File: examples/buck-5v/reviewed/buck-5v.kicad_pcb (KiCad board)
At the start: 2 copper layers, 126 x 56 mm, 11 parts, among them J1 12V IN, J2 5V OUT, U1 LM2596S-5

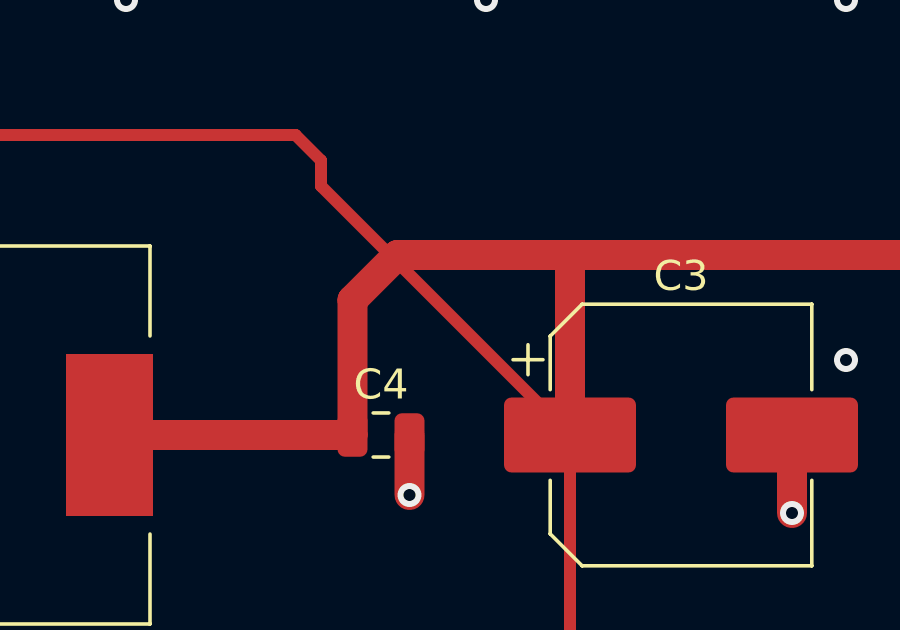
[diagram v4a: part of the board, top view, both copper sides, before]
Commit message: A net may not cross its own copper
The reviewer looked at the plots, saw tracks driven through each other, and
asked whether the other checks were really passing. Both halves of the
answer were worth keeping. Measured directly - every pair of same-layer
segments on every reviewed board - there is not one crossing between
different nets: DRC reports zero errors, zero shorts, zero unconnected, and
it is not being fooled. What the plots show is a net crossing *itself*:
thirteen places on the FPGA board, one each on the op-amp and the buck.
Same potential, so DRC has nothing to say; no length ratio catches it; no
rule of ours looked. The checks were honest. The check list had a hole
exactly the shape of what the eye catches first.

route.self_crossing (new, warning, promoted by ai-generated) measures it:
two branches of one net crossing means the copper carries a redundant loop,
and a person never draws one. KiCad's demo corpus: 6 of 16 boards carry one
to three, at dense escapes.

_unlooped (new pass) is the fix, as a graph question: split every same-net
crossing so the X is a node, and while any cycle remains in the net's
copper, remove the longest junction-to-junction chain of the cycle -
connectivity is kept by definition, a cycle has two ways round, and the
amputated X becomes an ordinary corner. The clearance oracle now also
refuses to let _doglegged or _straighten draw a new X over their own net.

The cutter was wrong twice before it was right, both times the same lesson:
KiCad's connectivity is geometric, a track graph is endpoint topology, and
the difference is exactly a pad. The escape fan draws a micro-hook inside
an off-grid pad - the overlap is the connection - and the graph read it as
a dangling loop and amputated the pad's only feed. Nodes inside an own-net
pad are anchors now, a cycle wholly inside one pad is immune, and segments
passing over a pad are split so the feed is a node the cut must respect.

Self-crossings on the five reviewed boards: 0/0/0/0/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
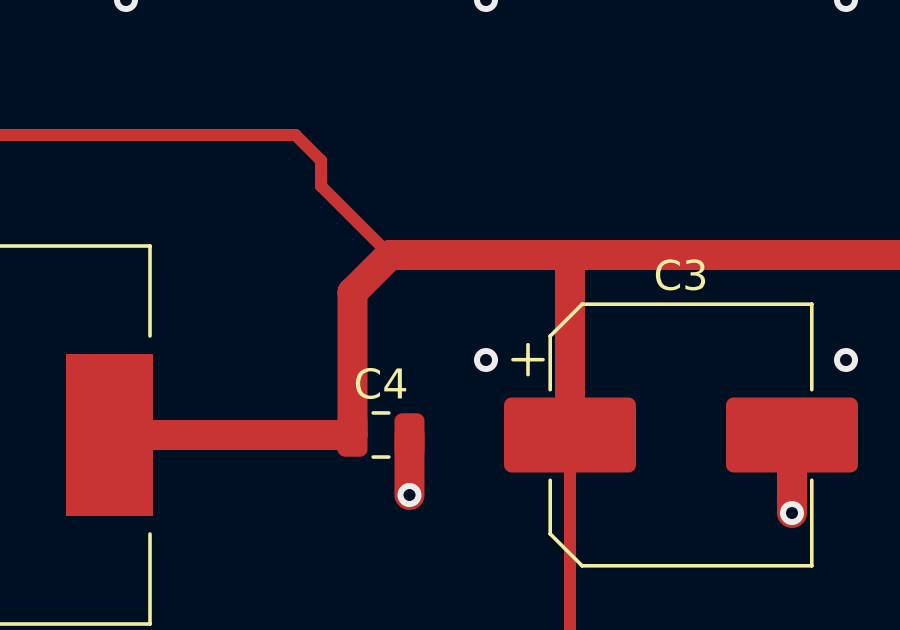
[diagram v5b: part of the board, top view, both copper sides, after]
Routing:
- net /+5V: track 131.6 -> 123.3 mm
- net GND: vias 84 -> 85
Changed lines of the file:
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@@
 	(gr_line (start 226.0 116.0) (end 100.0 116.0) (stroke (width 0.1) (type default)) (layer "Edge.Cuts"))
 	(gr_line (start 100.0 116.0) (end 100.0 60.0) (stroke (width 0.1) (type default)) (layer "Edge.Cuts"))
+	(segment (start 110.0 77.0) (end 110.0 108.5) (width 1.0) (layer "F.Cu") (net 1))
+	(segment (start 110.0 108.5) (end 111.5 110.0) (width 1.0) (layer "F.Cu") (net 1))
+	(segment (start 111.5 110.0) (end 116.0 110.0) (width 1.0) (layer "F.Cu") (net 1))
+	(segment (start 116.0 110.0) (end 210.0 110.0) (width 1.0) (layer "F.Cu") (net 1))
+	(segment (start 210.0 110.0) (end 219.5 110.0) (width 1.0) (layer "F.Cu") (net 1))
+	(segment (start 219.5 110.0) (end 221.0 108.5) (width 1.0) (layer "F.Cu") (net 1))
+	(segment (start 221.0 108.5) (end 221.0 96.0) (width 1.0) (layer "F.Cu") (net 1))
+	(segment (start 221.0 96.0) (end 216.0 91.0) (width 1.0) (layer "F.Cu") (net 1))
+	(segment (start 154.35 72.0) (end 151.0 72.0) (width 1.0) (layer "F.Cu") (net 1))
+	(segment (start 154.35 75.4) (end 154.35 80.0) (width 1.0) (layer "F.Cu") (net 1))
+	(segment (start 163.5 72.0) (end 163.5 80.0) (width 1.0) (layer "F.Cu") (net 1))
+	(segment (start 135.7 72.0) (end 135.7 74.6) (width 1.0) (layer "F.Cu") (net 1))
+	(segment (start 150.0 66.05) (end 150.0 64.4) (width 1.0) (layer "F.Cu") (net 1))
+	(segment (start 160.0 96.0) (end 160.0 91.0) (width 1.0) (layer "F.Cu") (net 1))
+	(segment (start 190.95 96.0) (end 190.95 98.0) (width 1.0) (layer "F.Cu") (net 1))
+	(segment (start 203.7 96.0) (end 203.7 98.6) (width 1.0) (layer "F.Cu") (net 1))
+	(segment (start 207.9375 106.0) (end 207.938 110.0) (width 0.4) (layer "F.Cu") (net 1))
 	(segment (start 110.0 72.0) (end 118.0 64.0) (width 1.0) (layer "F.Cu") (net 2))
 	(segment (start 118.0 64.0) (end 128.3 64.0) (width 1.0) (layer "F.Cu") (net 2))
@@
 	(segment (start 187.15 86.0) (end 188.0 86.85) (width 0.4) (layer "F.Cu") (net 3))
 	(segment (start 188.0 86.85) (end 188.0 87.7) (width 0.4) (layer "F.Cu") (net 3))
-	(segment (start 188.0 87.7) (end 196.3 96.0) (width 0.4) (layer "F.Cu") (net 3))
+	(segment (start 188.0 87.7) (end 190.3 90.0) (width 0.4) (layer "F.Cu") (net 3))
 	(segment (start 180.95 96.0) (end 189.05 96.0) (width 1.0) (layer "F.Cu") (net 3))
-	(segment (start 189.05 96.0) (end 189.05 91.5) (width 1.0) (layer "F.Cu") (net 3))
-	(segment (start 189.05 91.5) (end 190.55 90.0) (width 1.0) (layer "F.Cu") (net 3))
-	(segment (start 190.55 90.0) (end 196.3 90.0) (width 1.0) (layer "F.Cu") (net 3))
+	(segment (start 189.05 96.0) (end 189.05 91.25) (width 1.0) (layer "F.Cu") (net 3))
+	(segment (start 189.05 91.25) (end 190.3 90.0) (width 1.0) (layer "F.Cu") (net 3))
+	(segment (start 190.3 90.0) (end 196.3 90.0) (width 1.0) (layer "F.Cu") (net 3))
 	(segment (start 196.3 90.0) (end 196.3 96.0) (width 1.0) (layer "F.Cu") (net 3))
 	(segment (start 196.3 90.0) (end 210.0 90.0) (width 1.0) (layer "F.Cu") (net 3))
@@
 	(segment (start 196.3 103.2125) (end 199.0875 106.0) (width 0.4) (layer "F.Cu") (net 3))
 	(segment (start 200.9125 106.0) (end 206.0625 106.0) (width 0.4) (layer "F.Cu") (net 4))
-	(segment (start 110.0 77.0) (end 110.0 108.5) (width 1.0) (layer "F.Cu") (net 1))
-	(segment (start 110.0 108.5) (end 111.5 110.0) (width 1.0) (layer "F.Cu") (net 1))
-	(segment (start 111.5 110.0) (end 116.0 110.0) (width 1.0) (layer "F.Cu") (net 1))
-	(segment (start 116.0 110.0) (end 210.0 110.0) (width 1.0) (layer "F.Cu") (net 1))
-	(segment (start 210.0 110.0) (end 219.5 110.0) (width 1.0) (layer "F.Cu") (net 1))
-	(segment (start 219.5 110.0) (end 221.0 108.5) (width 1.0) (layer "F.Cu") (net 1))
-	(segment (start 221.0 108.5) (end 221.0 96.0) (width 1.0) (layer "F.Cu") (net 1))
-	(segment (start 221.0 96.0) (end 216.0 91.0) (width 1.0) (layer "F.Cu") (net 1))
-	(segment (start 154.35 72.0) (end 151.0 72.0) (width 1.0) (layer "F.Cu") (net 1))
-	(segment (start 154.35 75.4) (end 154.35 80.0) (width 1.0) (layer "F.Cu") (net 1))
-	(segment (start 163.5 72.0) (end 163.5 80.0) (width 1.0) (layer "F.Cu") (net 1))
-	(segment (start 135.7 72.0) (end 135.7 74.6) (width 1.0) (layer "F.Cu") (net 1))
-	(segment (start 150.0 66.05) (end 150.0 64.4) (width 1.0) (layer "F.Cu") (net 1))
-	(segment (start 160.0 96.0) (end 160.0 91.0) (width 1.0) (layer "F.Cu") (net 1))
-	(segment (start 190.95 96.0) (end 190.95 98.0) (width 1.0) (layer "F.Cu") (net 1))
-	(segment (start 203.7 96.0) (end 203.7 98.6) (width 1.0) (layer "F.Cu") (net 1))
-	(segment (start 207.9375 106.0) (end 207.938 110.0) (width 0.4) (layer "F.Cu") (net 1))
 	(via (at 169.5 67.5) (size 0.8) (drill 0.4) (layers "F.Cu" "B.Cu") (net 1))
 	(via (at 169.5 72.0) (size 0.8) (drill 0.4) (layers "F.Cu" "B.Cu") (net 1))
@@
 	(via (at 145.5 93.5) (size 0.8) (drill 0.4) (layers "F.Cu" "B.Cu") (net 1))
 	(via (at 157.5 93.5) (size 0.8) (drill 0.4) (layers "F.Cu" "B.Cu") (net 1))
+	(via (at 193.5 93.5) (size 0.8) (drill 0.4) (layers "F.Cu" "B.Cu") (net 1))
 	(via (at 205.5 93.5) (size 0.8) (drill 0.4) (layers "F.Cu" "B.Cu") (net 1))
 	(via (at 217.5 93.5) (size 0.8) (drill 0.4) (layers "F.Cu" "B.Cu") (net 1))

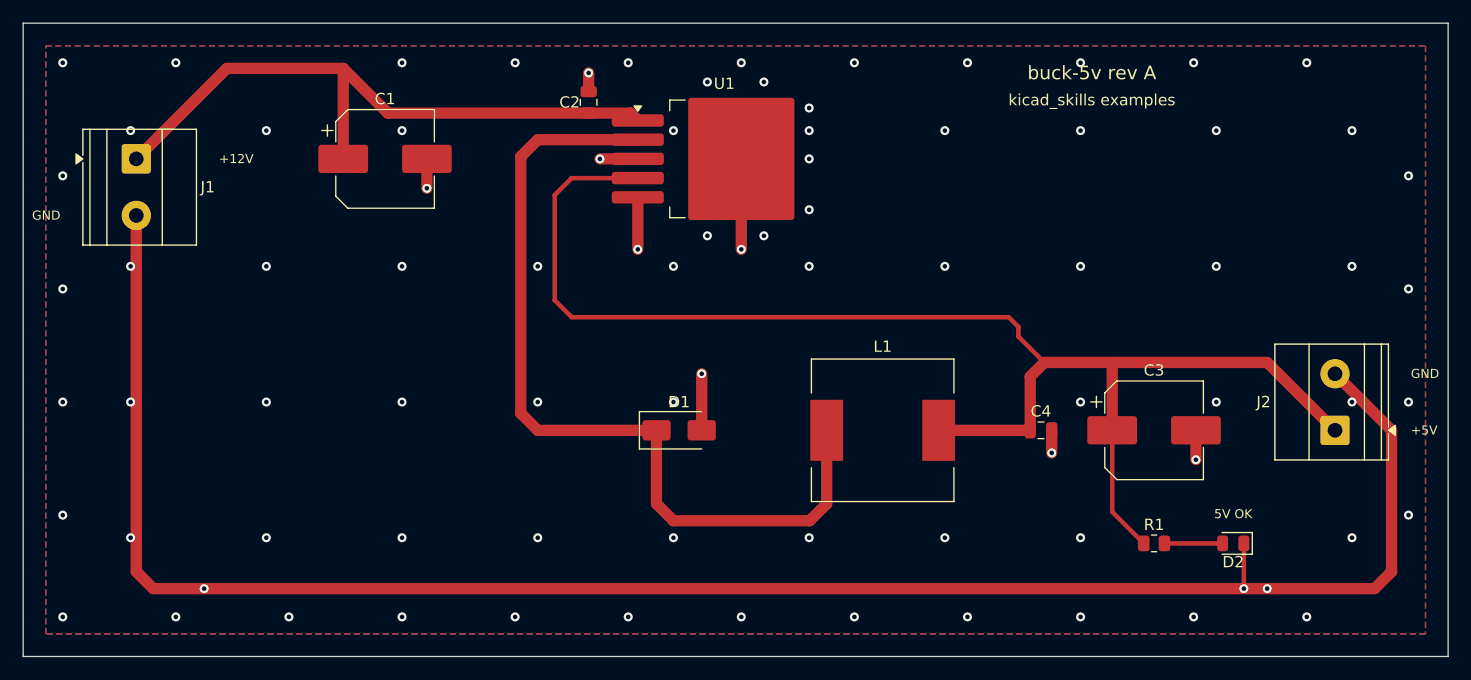
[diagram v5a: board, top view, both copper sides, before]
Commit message: Treat the ground plane as part of the drawing
Six reviewer circles, five of them the plane seen from different corners.
The pour now stops 1.2 mm inside the outline so an edge-hugging trace
keeps shell copper outside it; dead-end tongues narrower than 0.9 mm
retract instead of tapering to an acid-trap point in a bent corner; every
piece of the front pour over 8 mm2 holds a stitching via of its own,
placed before the orphan drop so a fenced-off strip gets a via instead of
staying a blank; and zone clearance comes down from 0.4 to 0.25, which is
what lets the plane flow between a 2.54 mm header's pins instead of
slotting the board top to bottom.

The round-twelve tee learns one manner: within two millimetres of the
goal it stands aside, so a rail flows through a bypass capacitor's pad
instead of feeding it by a stub - the carrier's bulk capacitor also moves
onto the VSYS run it was a millimetre south of. And
readability.margin_intrusion now measures symbol fields, power symbols
included: zero findings across KiCad's 18 demo sheets, one real catch on
our own motor sheet, whose power connector - like the FPGA board's -
moves in from the sheet edge so its printed name clears the frame.

Co-Authored-By: Claude Fable 5 <noreply@anthropic.com>
Claude-Session: https://claude.ai/code/session_01DUj7Ltu92tWg159mCSacwY
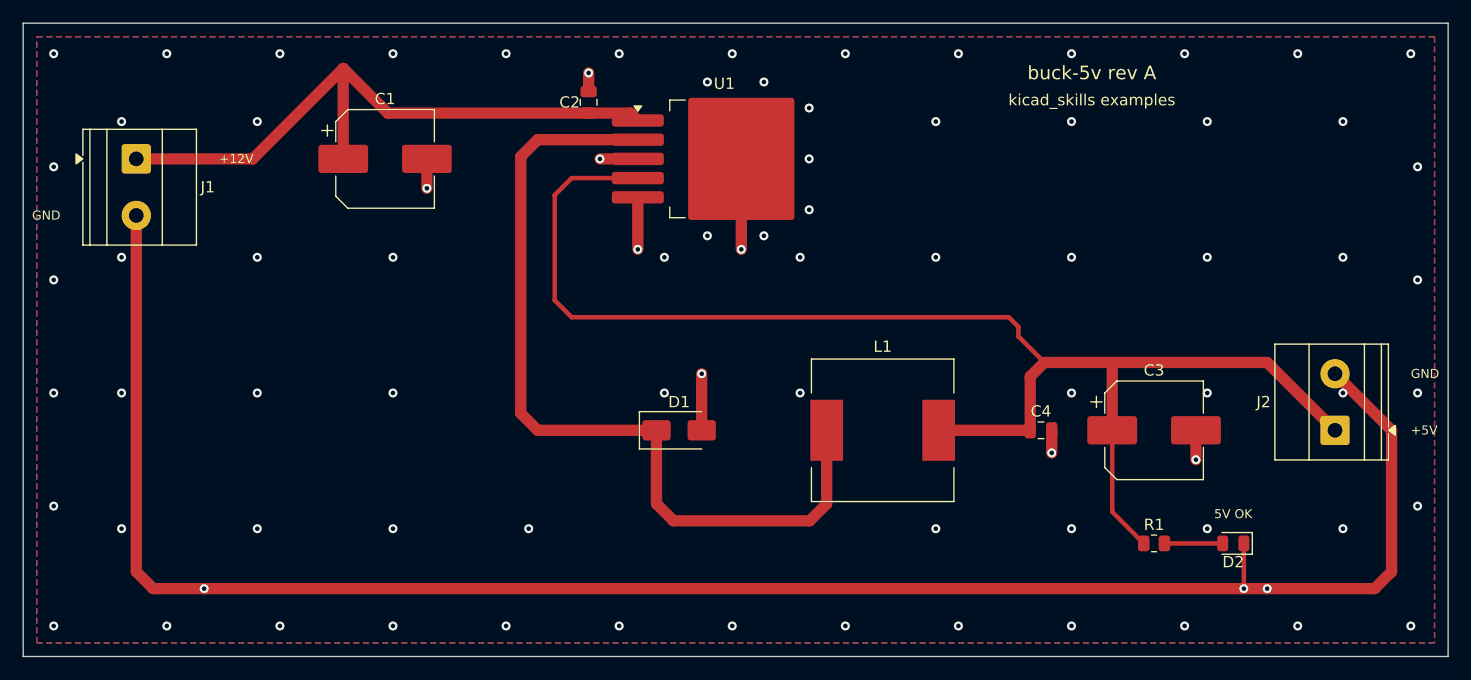
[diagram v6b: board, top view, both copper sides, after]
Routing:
- net GND: vias 85 -> 83

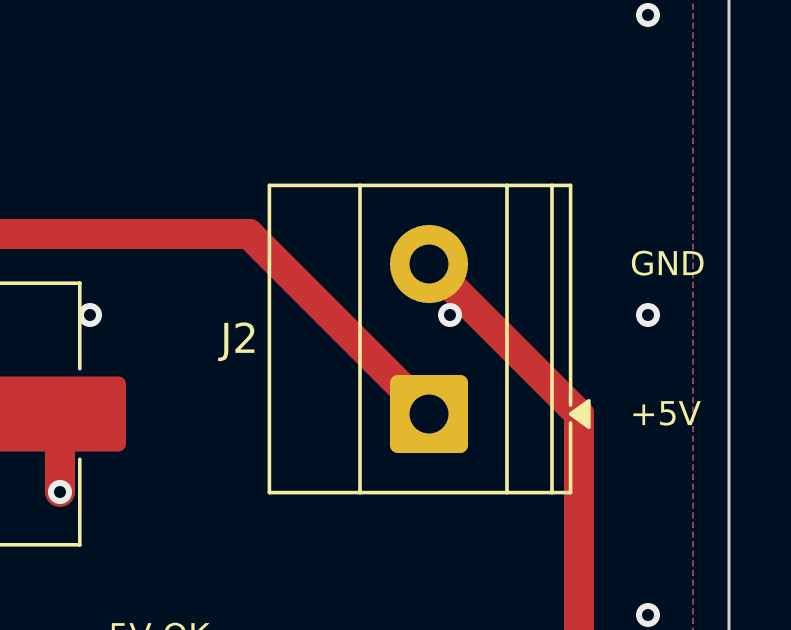
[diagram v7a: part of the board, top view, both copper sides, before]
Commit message: Keep vias out of the lands they would drain
The reviewer's next one, and it is not one board's problem: vias were
landing inside surface-mount lands across the set. A hole in a land is a
hole solder wicks down during reflow - the joint above it starves, and
nothing on the assembled board tells that apart from a cold one.
Via-in-pad is a real technique and a filled-and-capped process, not a
drawing; a layout that has not specified the process may not draw it.

The router was the source. `_blocked` skips a route's own net, so
nothing stopped a layer change from happening on the very land the route
started at, and eighteen vias across three boards sat in one. Pads are
now marked as pads in the obstacle list and every one of them, whoever
owns it, is a cell where a via may not go - so an escape that has to
reach the plane leaves the land first and turns its via beside it. The
stitching pass kept ground vias a via-radius from ground lands where it
kept signal ones a radius plus clearance; both are the same distance
now, because the plane gains nothing from touching a land it can reach a
stub away.

`via.in_pad` measures the copper gap from every via to every land and
reports what is left. The exposed thermal pad under a package is exempt
- the via array in one is the datasheet's own answer, and nothing a
signal reaches is four square millimetres. It blocks under the
ai-generated policy: a generated board has no reason to draw this.

The test fixture had one too, a via twenty-five microns into C1's ground
land; it moves three tenths of a millimetre and the board is DRC clean
on both matrix versions as before.

Co-Authored-By: Claude Fable 5 <noreply@anthropic.com>
Claude-Session: https://claude.ai/code/session_01DUj7Ltu92tWg159mCSacwY
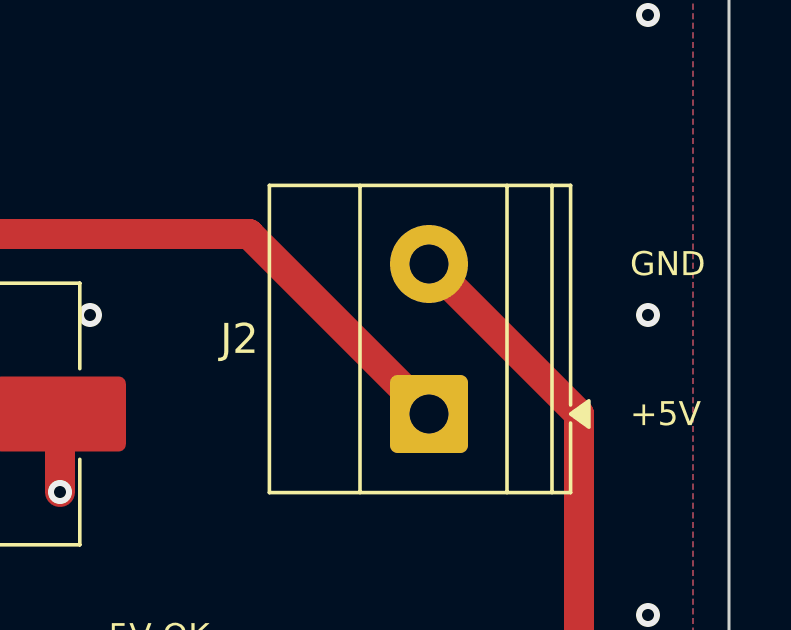
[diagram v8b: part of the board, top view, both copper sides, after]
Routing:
- net GND: vias 83 -> 82
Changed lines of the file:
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@@
 	(via (at 192.7 92.7) (size 0.8) (drill 0.4) (layers "F.Cu" "B.Cu") (net 1))
 	(via (at 204.7 92.7) (size 0.8) (drill 0.4) (layers "F.Cu" "B.Cu") (net 1))
-	(via (at 216.7 92.7) (size 0.8) (drill 0.4) (layers "F.Cu" "B.Cu") (net 1))
 	(via (at 108.7 104.7) (size 0.8) (drill 0.4) (layers "F.Cu" "B.Cu") (net 1))
 	(via (at 120.7 104.7) (size 0.8) (drill 0.4) (layers "F.Cu" "B.Cu") (net 1))
